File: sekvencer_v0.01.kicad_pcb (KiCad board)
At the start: 2 copper layers, 79.2 x 91.4 mm, 98 parts, among them J1 AVR_ISP_01X06, J10 50V_OUT, J11 BIAS, J12 50V_GND, J13 TERMISTOR, J14 50V_GND, J15 50V_GND, J16 50V_GND, J2 PTT, J3 SWR, J4 POWER, J5 LCD, J6 RX_REL, J7 TX_REL, J8 FAN, J9 50V_IN, Q1 BC857, Q2 Q_NMOS_DGS, Q3 BSS138, Q4 IRLML0030TRPBF, Q5 BBS3002-TL-1E, Q6 BSS138, U1 ATmega328P-AU, U2 LP2950-5.0_TO252, U3 LM2576HVS-12, U4 LTC6101AHS5, Y1 16MHz

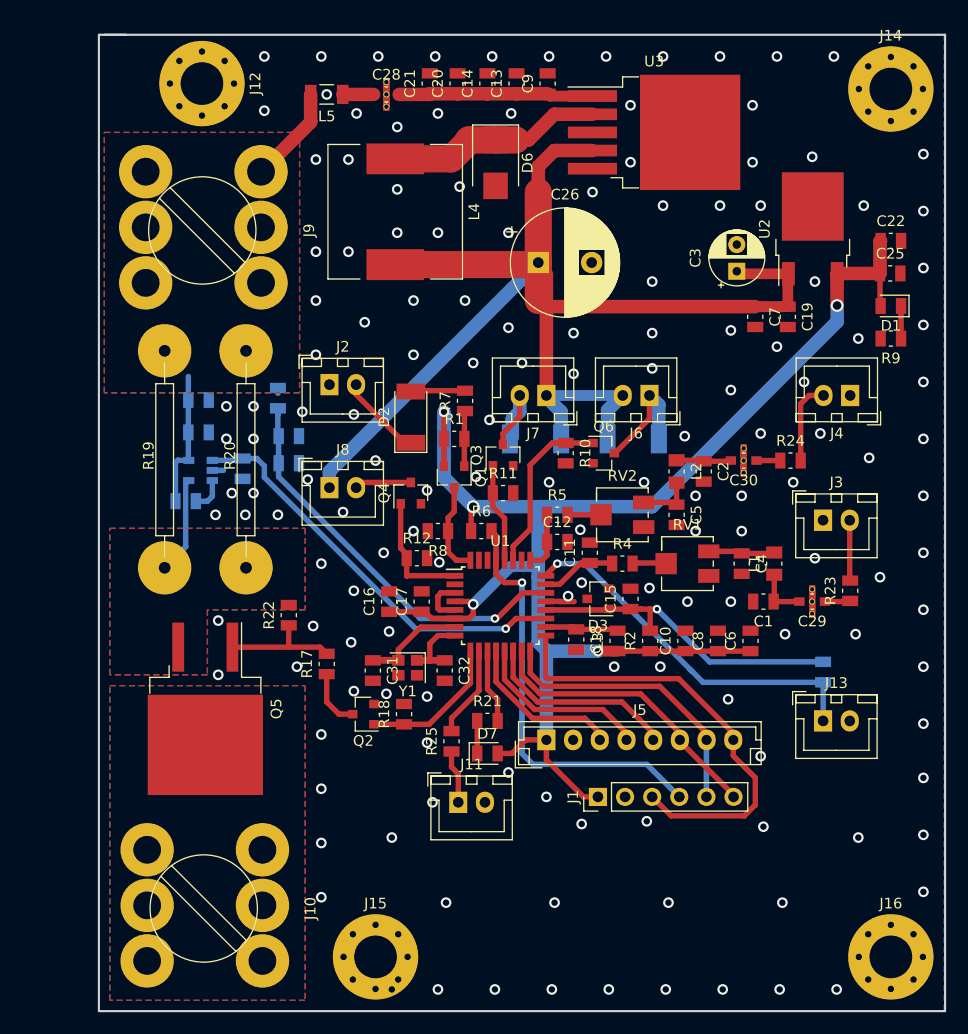
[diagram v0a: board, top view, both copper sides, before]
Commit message: refactored second version, added bias circuit, fixed layout
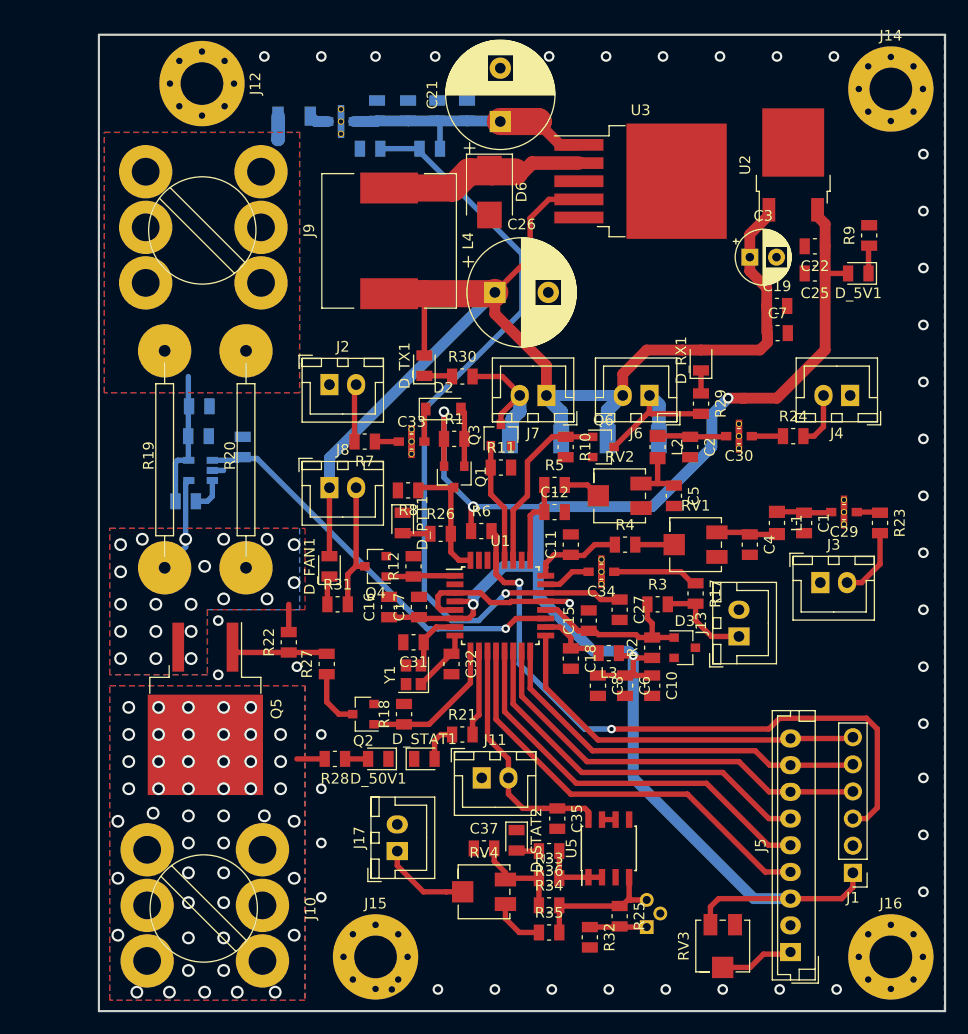
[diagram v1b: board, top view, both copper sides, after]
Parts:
- removed D1: 5V_LED, LED_SMD:LED_0805_2012Metric
- removed D7: STAT_LED, LED_SMD:LED_0805_2012Metric
- added C33: NFM21CC223R1H3D, EMI_Suppression_Filters_Cap_Type:NFM21C_Series, F.Cu at (183.7, 86.4)
- added C34: NFM21CC223R1H3D, EMI_Suppression_Filters_Cap_Type:NFM21C_Series, F.Cu at (201.5, 98.6)
- added C35: 2u2, Capacitor_SMD:C_0805_2012Metric, F.Cu at (197.4, 121.7)
- added C37: 1u, Capacitor_SMD:C_0805_2012Metric, F.Cu at (190.5, 124.5)
- added D_50V1: LH R974-LP-1, LED_SMD:LED_0805_2012Metric, F.Cu at (180.6, 116.1)
- added D_5V1: LH R974-LP-1, LED_SMD:LED_0805_2012Metric, F.Cu at (225.6, 70.6)
- added D_FAN1: LH R974-LP-1, LED_SMD:LED_0805_2012Metric, F.Cu at (176.0, 98.0)
- added D_PTT1: LH R974-LP-1, LED_SMD:LED_0805_2012Metric, F.Cu at (182.9, 94.0)
- added D_RX1: LH R974-LP-1, LED_SMD:LED_0805_2012Metric, F.Cu at (210.8, 78.7)
- added D_STAT1: LH R974-LP-1, LED_SMD:LED_0805_2012Metric, F.Cu at (184.9, 116.1)
- added D_STAT2: LH R974-LP-1, LED_SMD:LED_0805_2012Metric, F.Cu at (193.5, 123.7)
- added D_TX1: LH R974-LP-1, LED_SMD:LED_0805_2012Metric, F.Cu at (184.9, 79.2)
- added J17: BIAS, Connector_JST:JST_XH_B02B-XH-A_1x02_P2.50mm_Vertical, F.Cu at (182.4, 124.7)
- added Q7: BC847, Package_TO_SOT_THT:TO-92, B.Cu at (205.7, 131.8)
- added R26: 1k, Resistor_SMD:R_0805_2012Metric, F.Cu at (186.4, 95.0)
- added R27: 12k, Resistor_SMD:R_0805_2012Metric, F.Cu at (175.8, 107.2)
- added R28: 18k, Resistor_SMD:R_0805_2012Metric, F.Cu at (176.5, 116.1)
- added R29: 3k9, Resistor_SMD:R_0805_2012Metric, F.Cu at (210.8, 82.8)
- added R30: 3k9, Resistor_SMD:R_0805_2012Metric, F.Cu at (188.5, 80.3)
- added R31: 3k9, Resistor_SMD:R_0805_2012Metric, F.Cu at (176.8, 101.6)
- added R32: 2k2, Resistor_SMD:R_0805_2012Metric, F.Cu at (200.4, 132.8)
- added R33: 10R, Resistor_SMD:R_0805_2012Metric, F.Cu at (196.6, 127.3)
- added R34: 1k, Resistor_SMD:R_0805_2012Metric, F.Cu at (196.6, 129.8)
- added R35: 220R, Resistor_SMD:R_0805_2012Metric, F.Cu at (196.6, 132.3)
- added R36: R, Resistor_SMD:R_0805_2012Metric, F.Cu at (196.6, 124.7)
- added RV3: 10k, Potentiometer_SMD:Potentiometer_Bourns_3214J_Horizontal, F.Cu at (212.9, 133.6)
- added RV4: 10k, Potentiometer_SMD:Potentiometer_Bourns_3214J_Horizontal, F.Cu at (190.5, 128.5)
- added U5: LP2951ACD-3.3R2G, Package_SO:SOIC-8_3.9x4.9mm_P1.27mm, F.Cu at (202.2, 124.5)
- C13, C14, C20, C28, C9, L5: moved to B.Cu
- C21: footprint Capacitor_SMD:C_0805_2012Metric -> Capacitor_THT:CP_Radial_D10.0mm_P5.00mm
- C27, R3: moved to F.Cu
- D2: footprint Diode_SMD:D_MELF -> Diode_SMD:D_SOD-123
- J11: value BIAS -> BIAS_DIRECT
- J5: footprint Connector_JST:JST_EH_B08B-EH-A_1x08_P2.50mm_Vertical -> Connector_JST:JST_EH_B09B-EH-A_1x09_P2.50mm_Vertical
- R13: value 330R -> 499R
- R14: value 2k -> 10k
- R17: value 12k -> 22k
- R19, R20: value 0R01 -> 0R005
- R2: value 180R -> 1k
- R25: value 1k -> 1k2
- moved R17 35.2 mm to (210.3, 100.6), turned to 270 degrees
- moved C27 33.9 mm to (203.2, 102.1), turned to 270 degrees
- moved J5 30.3 mm to (219.2, 134.2), turned to 90 degrees
- moved R16 28.0 mm to (179.8, 58.9), turned to 180 degrees
- moved R15 27.4 mm to (185.4, 58.9), turned to 180 degrees
- moved J1 24.9 mm to (225.0, 126.7), turned to 180 degrees
- moved R25 22.7 mm to (203.2, 130.8), turned to 270 degrees
- moved R3 16.7 mm to (206.8, 101.6), turned to 0 degrees
- moved C9 16.2 mm to (180.5, 55.4)
- moved C6 12.5 mm to (203.7, 109.2), turned to 270 degrees
- moved C8 12.0 mm to (201.2, 109.2), turned to 270 degrees
- moved J13 11.2 mm to (214.4, 104.6), turned to 90 degrees
- moved C13 10.5 mm to (183.4, 55.4)
- moved R7 10.1 mm to (179.3, 86.4), turned to 180 degrees
- moved R9 9.86 mm to (226.6, 67.1), turned to 90 degrees
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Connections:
- D2 pad 1: Net-(D2-Pad1) -> Net-(C33-Pad3)
- J1 pad 3: /DB7 -> /RESET
- J1 pad 4: /RESET -> /DB5
- J1 pad 6: /DB5 -> /DB7
- J11 pad 1: Net-(J11-Pad1) -> GND
- J11 pad 2: GND -> /MCU_BIAS
- J13 pad 1: /ADC_TEMP -> Net-(J13-Pad1)
- J2 pad 2: Net-(D2-Pad1) -> Net-(J2-Pad2)
- J5 pad 1: +5V -> Net-(J5-Pad1)
- J5 pad 3: /RS -> +5V
- J5 pad 4: /E -> /RS
- J5 pad 5: /DB4 -> /E
- J5 pad 6: /DB5 -> /DB4
- J5 pad 7: /DB6 -> /DB5
- J5 pad 8: /DB7 -> /DB6
- Q1 pad 1: Net-(Q1-Pad1) -> Net-(D2-Pad2)
- R1 pad 2: Net-(Q1-Pad1) -> Net-(D2-Pad2)
- R15 pad 1: +50V -> Net-(C13-Pad1)
- R17 pad 1: Net-(Q2-Pad3) -> Net-(C34-Pad1)
- R17 pad 2: Net-(Q5-Pad1) -> Net-(J13-Pad1)
- R21 pad 2: /STATUS_LED -> /STATUS_LED1
- R25 pad 1: Net-(J11-Pad1) -> Net-(Q7-Pad3)
- R25 pad 2: /MCU_BIAS -> Net-(Q7-Pad1)
- R3 pad 2: /ADC_TEMP -> Net-(J13-Pad1)
- R7 pad 1: Net-(Q1-Pad1) -> Net-(C33-Pad1)
- R7 pad 2: Net-(D2-Pad2) -> Net-(J2-Pad2)
- U1 pad 10: /MCU_BIAS -> /STATUS_LED1
- U1 pad 11: /STATUS_LED -> /MCU_BIAS
- U1 pad 2: (no net) -> Net-(U1-Pad2)
- U1 pad 23: /ADC_SWR -> /ADC_TEMP
- U1 pad 24: /ADC_TEMP -> /ADC_SWR
- U1 pad 26: (no net) -> Net-(U1-Pad26)
- U1 pad 30: (no net) -> Net-(U1-Pad30)
- U1 pad 31: (no net) -> Net-(U1-Pad31)
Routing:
- net /ADC_UCC: track 37.9 -> 74.0 mm
- net /ADC_TEMP: track 34.9 -> 4.50 mm, vias 1 -> 0
- net /RS: track 15.2 -> 39.9 mm
- net +5V: track 146.6 -> 170.7 mm
- net /RESET: track 39.4 -> 61.3 mm, vias 1 -> 2
- net /E: track 16.8 -> 37.6 mm
- net /DB4: track 18.4 -> 35.4 mm
- net /MCU_BIAS: track 8.56 -> 23.6 mm
- net +2V5: track 30.6 -> 16.8 mm, vias 1 -> 0
- net Net-(Q7-Pad3): track 0.00 -> 12.8 mm
- net /DB5: track 27.4 -> 39.0 mm
- net /DB6: track 26.9 -> 36.7 mm
- net Net-(C37-Pad2): track 0.00 -> 9.08 mm
- net Net-(J13-Pad1): track 0.00 -> 8.89 mm
- net Net-(J17-Pad1): track 0.00 -> 8.50 mm
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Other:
- outline, holes or cut-outs redrawn

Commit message: oficial second version, fixed previous commit
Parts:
- added J18: 50V_GND, MountingHole:MountingHole_3.2mm_M3_Pad_Via, F.Cu at (151.4, 115.3)
- D4, D5: moved to F.Cu
- J12, J14, J16: footprint MountingHole:MountingHole_4mm_Pad_Via -> MountingHole:MountingHole_4.3mm_M4_Pad_Via
- J15: footprint MountingHole:MountingHole_4mm_Pad_Via -> MountingHole:MountingHole_3.2mm_M3_Pad_Via
- moved J15 19.0 mm to (177.8, 115.8)
- moved D_50V1 18.1 mm to (181.6, 134.1)
- moved R28 18.1 mm to (177.3, 134.1)
- moved D5 11.5 mm to (186.9, 78.2), turned to 270 degrees
- moved R29 11.1 mm to (207.0, 72.4), turned to 0 degrees
- moved D4 10.2 mm to (205.0, 75.9)
- moved D_RX1 10.1 mm to (202.9, 72.4), turned to 180 degrees
- moved C32 5.40 mm to (183.9, 111.3), turned to 180 degrees
- moved R30 5.09 mm to (183.4, 80.5)
- moved C34 4.92 mm to (206.2, 99.8)
- moved J17 3.84 mm to (182.9, 128.5), turned to 180 degrees
- moved D_TX1 3.42 mm to (182.6, 76.7)
- moved C27 3.06 mm to (200.9, 100.1), turned to 0 degrees
- moved R18 2.95 mm to (183.4, 114.8), turned to 270 degrees
- moved J1 2.29 mm to (225.0, 124.5)
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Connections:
- J1 pad 3: /RESET -> /DB5
- J1 pad 4: /DB5 -> /DB6
- J1 pad 5: /DB6 -> /DB7
- J1 pad 6: /DB7 -> /RESET
- J13 pad 1: Net-(J13-Pad1) -> GND
- J13 pad 2: GND -> Net-(J13-Pad2)
- R17 pad 2: Net-(J13-Pad1) -> Net-(J13-Pad2)
- R3 pad 2: Net-(J13-Pad1) -> Net-(J13-Pad2)
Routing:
- net /RESET: track 61.3 -> 48.7 mm
- net Net-(J13-Pad1): track 8.89 -> 0.00 mm
- net Net-(J13-Pad2): track 0.00 -> 7.24 mm
- net +12V: track 119.2 -> 125.2 mm
- net Net-(C34-Pad1): track 8.07 -> 2.70 mm
- net /ADC_TEMP: track 4.50 -> 9.79 mm
- net Net-(C32-Pad1): track 5.87 -> 9.41 mm
- net Net-(J17-Pad1): track 8.50 -> 5.62 mm
- net +2V5: track 16.8 -> 14.4 mm
- net Net-(D_STAT1-Pad2): track 3.60 -> 5.66 mm
- net /STATUS_LED1: track 8.09 -> 6.05 mm
- net Net-(D5-Pad2): track 13.1 -> 15.0 mm
- net /MCU_SUPPLY: track 13.6 -> 15.4 mm
- net Net-(Q2-Pad3): track 5.50 -> 3.93 mm
- net /ADC_UCC: track 74.0 -> 72.6 mm
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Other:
- board size 79.2 x 91.4 mm -> 86.4 x 91.4 mm

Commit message: third version, sent to fabrication in allpcb
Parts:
- removed D_STAT2: LH R974-LP-1, LED_SMD:LED_0805_2012Metric
- added C36: NFM21CC223R1H3D, EMI_Suppression_Filters_Cap_Type:NFM21C_Series, F.Cu at (187.3, 133.0)
- added C38: NFM21CC223R1H3D, EMI_Suppression_Filters_Cap_Type:NFM21C_Series, B.Cu at (159.3, 88.5)
- added C39: NFM21CC223R1H3D, EMI_Suppression_Filters_Cap_Type:NFM21C_Series, B.Cu at (156.5, 85.7)
- added D_3V3: LH R974-LP-1, LED_SMD:LED_0805_2012Metric, F.Cu at (193.5, 123.6)
- added J19: 50V_GND, MountingHole:MountingHole_3.2mm_M3_Pad_Via, F.Cu at (151.4, 134.6)
- added L6: BLM31PG500SN1L, Capacitor_SMD:C_1206_3216Metric, F.Cu at (182.4, 133.1)
- added L7: BLM31PG500SN1L, Capacitor_SMD:C_1206_3216Metric, B.Cu at (156.5, 91.4)
- added L8: BLM31PG500SN1L, Capacitor_SMD:C_1206_3216Metric, B.Cu at (159.3, 84.3)
- added TP1: ADC_UCC, TestPoint:TestPoint_Pad_D2.0mm, F.Cu at (199.9, 99.9)
- added TP2: +5V, TestPoint:TestPoint_Pad_D2.0mm, F.Cu at (222.5, 75.0)
- added TP3: +12V, TestPoint:TestPoint_Pad_D2.0mm, F.Cu at (211.2, 69.8)
- added TP4: ADC ICC, TestPoint:TestPoint_Pad_D2.0mm, B.Cu at (170.6, 90.0)
- added TP5: GND, TestPoint:TestPoint_Pad_D2.0mm, F.Cu at (199.7, 76.5)
- C31, C32: value 22p -> 15p
- J12, J14, J16: footprint MountingHole:MountingHole_4.3mm_M4_Pad_Via -> MountingHole:MountingHole_3.2mm_M3_Pad_Via
- R36: value R -> 470R
- Y1: footprint Crystal:Crystal_SMD_2520-4Pin_2.5x2.0mm -> KLALIB_Crystal:Crystal_SMD_2520-4Pin_2.5x2.0mm
- moved J12 11.7 mm to (152.4, 53.3)
- moved C23 6.20 mm to (168.9, 86.6), turned to 270 degrees
- moved R14 5.36 mm to (164.4, 90.9), turned to 90 degrees
- moved R31 3.81 mm to (176.8, 97.8)
- moved R7 3.78 mm to (181.9, 83.6), turned to 90 degrees
- moved D_50V1 3.69 mm to (181.4, 137.8)
- moved R28 3.69 mm to (177.0, 137.8)
- moved D_FAN1 3.31 mm to (175.8, 94.7)
- moved J2 3.14 mm to (178.3, 78.9), turned to 180 degrees
- moved C32 3.07 mm to (186.2, 109.3), turned to 270 degrees
- moved J3 2.90 mm to (224.8, 100.3), turned to 180 degrees
- moved J8 2.62 mm to (178.3, 89.4), turned to 180 degrees
- moved J11 2.61 mm to (192.8, 118.6), turned to 180 degrees
- moved U4 2.55 mm to (162.9, 86.7), turned to 90 degrees
- moved C24 2.46 mm to (166.1, 86.5), turned to 270 degrees
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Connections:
- C35 pad 1: /MCU_BIAS -> +5V
- J11 pad 1: GND -> /MCU_BIAS
- J11 pad 2: /MCU_BIAS -> GND
- J2 pad 1: GND -> Net-(J2-Pad1)
- J2 pad 2: Net-(J2-Pad2) -> GND
- J3 pad 1: GND -> Net-(J3-Pad1)
- J3 pad 2: Net-(J3-Pad2) -> GND
- J8 pad 1: +12V -> Net-(J8-Pad1)
- J8 pad 2: Net-(J8-Pad2) -> +12V
- Q4 pad 3: Net-(J8-Pad2) -> Net-(J8-Pad1)
- Q5 pad 3: Net-(Q5-Pad3) -> Net-(L7-Pad1)
- R13 pad 1: Net-(R13-Pad1) -> Net-(C38-Pad1)
- R13 pad 2: +50V -> Net-(R13-Pad2)
- R19 pad 1: Net-(Q5-Pad3) -> Net-(L7-Pad1)
- R20 pad 1: Net-(Q5-Pad3) -> Net-(L7-Pad1)
- R22 pad 2: Net-(Q5-Pad3) -> Net-(L7-Pad1)
- R23 pad 2: Net-(J3-Pad2) -> Net-(J3-Pad1)
- R31 pad 2: Net-(J8-Pad2) -> Net-(J8-Pad1)
- R7 pad 2: Net-(J2-Pad2) -> Net-(J2-Pad1)
- RV4 pad 2: Net-(J17-Pad1) -> Net-(C36-Pad1)
- U4 pad 3: Net-(R13-Pad1) -> Net-(R13-Pad2)
- U4 pad 4: Net-(Q5-Pad3) -> Net-(C39-Pad1)
- U5 pad 3: Net-(U5-Pad3) -> /MCU_BIAS
- U5 pad 8: /MCU_BIAS -> +5V
- Y1 pad 2: Net-(C31-Pad1) -> GND
- Y1 pad 3: (no net) -> Net-(C31-Pad1)
- Y1 pad 4: (no net) -> GND
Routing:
- net GND: track 16.8 -> 35.6 mm, vias 41 -> 225
- net +5V: track 172.1 -> 186.0 mm, vias 5 -> 6
- net Net-(J8-Pad2): track 12.1 -> 0.00 mm
- net Net-(Q5-Pad3): track 11.7 -> 0.00 mm, vias 21 -> 0
- net /MCU_BIAS: track 23.6 -> 34.4 mm
- net Net-(J8-Pad1): track 0.00 -> 10.4 mm
- net Net-(J3-Pad1): track 0.00 -> 7.47 mm
- net Net-(J3-Pad2): track 6.71 -> 0.00 mm
- net Net-(C39-Pad1): track 0.00 -> 6.60 mm
- net Net-(J2-Pad1): track 0.00 -> 5.83 mm
- net Net-(J2-Pad2): track 5.40 -> 0.00 mm
- net Net-(L7-Pad1): track 0.00 -> 4.91 mm, vias 0 -> 21
- net Net-(C36-Pad1): track 0.00 -> 4.46 mm
- net /ADC_ICC: track 38.0 -> 42.1 mm
- net Net-(R13-Pad2): track 0.00 -> 3.82 mm
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- added copper zone on B.Cu, net Net-(L7-Pad1)
- added copper zone on F.Cu, net Net-(L7-Pad1)
- removed copper zone on B.Cu, net Net-(Q5-Pad3)
- removed copper zone on F.Cu, net Net-(Q5-Pad3)
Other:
- board text added: "+12V"
- board text added: "+50 V OUT"
- board text added: "+50V IN"
- board text added: "+5V"
- board text added: "ADC"
- board text added: "ADC ICC"
- board text added: "BIAS"
- board text added: "BIAS DIRECT"
- board text added: "FAN"
- board text added: "ISP"
- board text added: "LCD"
- board text added: "POWER"
- board text added: "PTT"
- board text added: "REL1"
- board text added: "REL2"
- board text added: "SWR"
- board text added: "TEMP"
- board text added: "UCC"

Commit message: added some docs and outputs
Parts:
- D2, D4, D5: value D -> 1N4148
- L1, L2: value 560n -> 470n
- Q2: value Q_NMOS_DGS -> BSS138

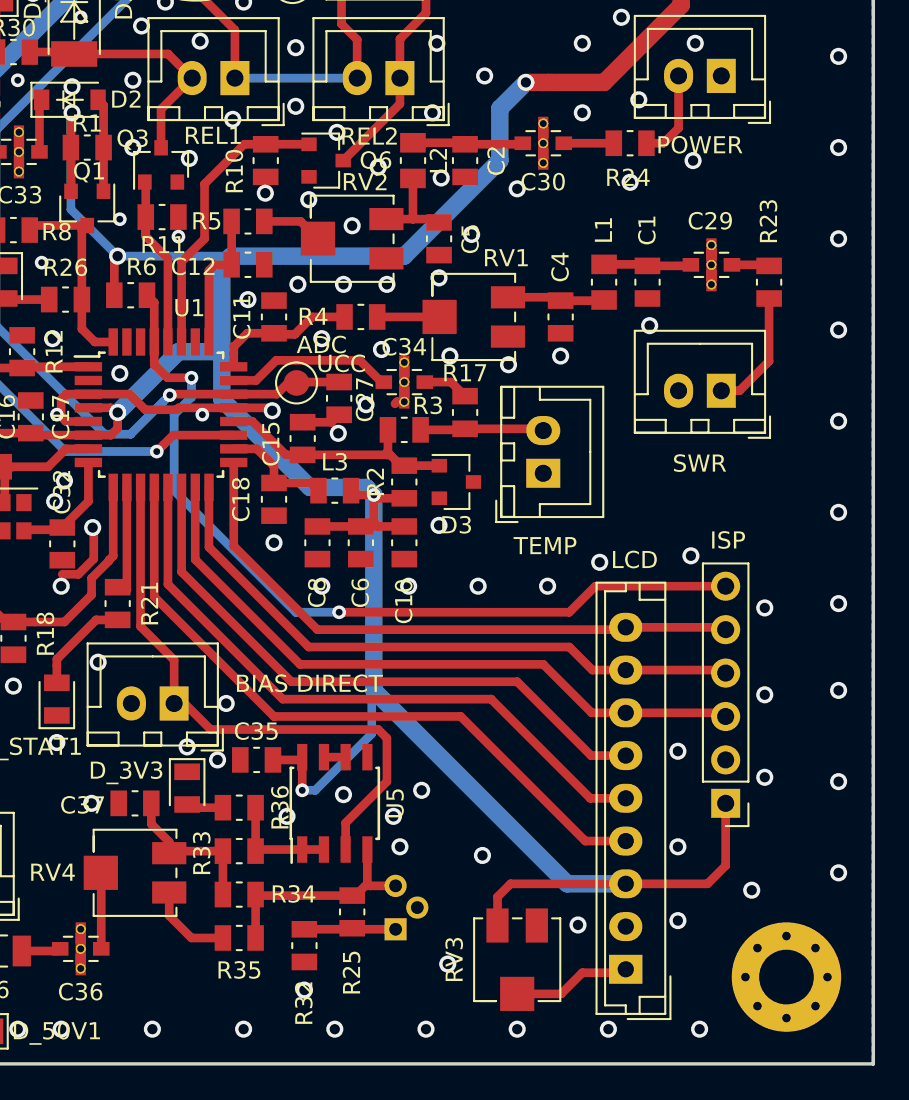
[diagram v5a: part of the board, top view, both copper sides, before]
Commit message: first revision, added resistor and diode in bias circuit
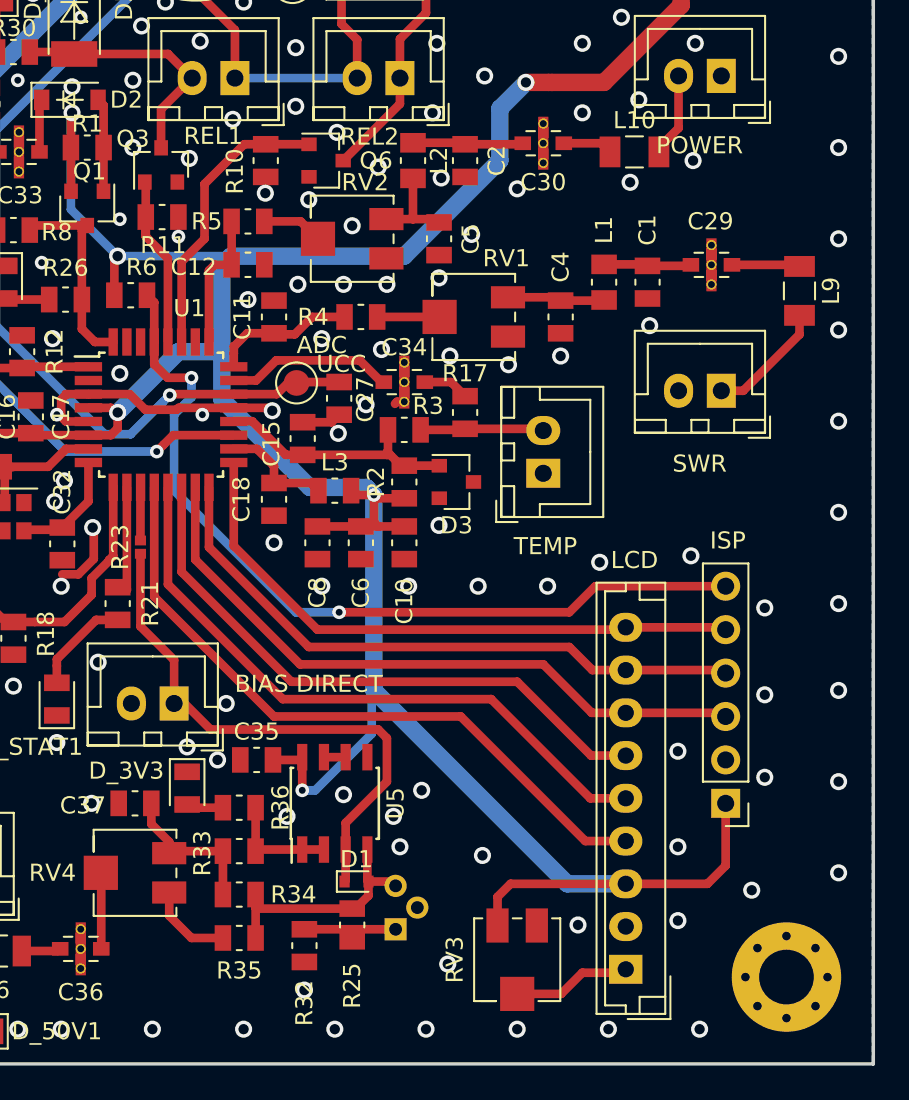
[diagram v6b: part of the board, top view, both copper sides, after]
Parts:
- removed R24: 1k, Resistor_SMD:R_0805_2012Metric
- added D1: BAS7002VH6327XTSA1, Diode_SMD:D_SOD-523, F.Cu at (203.5, 129.0)
- added L10: BLM31PG500SN1L, Capacitor_SMD:C_1206_3216Metric, F.Cu at (219.7, 86.4)
- added L9: BLM31PG500SN1L, Capacitor_SMD:C_1206_3216Metric, F.Cu at (229.4, 94.5)
- R23: value 1k -> 100k; footprint Resistor_SMD:R_0805_2012Metric -> Resistor_SMD:R_0402_1005Metric
- Y1: value 16MHz -> LFXTAL071268CUTT 16MHz
- moved R23 39.9 mm to (190.8, 109.5), turned to 90 degrees
- moved R25 0.76 mm to (203.2, 131.6)
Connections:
- J11 pad 1: /MCU_BIAS -> Net-(D1-Pad1)
- J14 pad 1: GND -> Net-(J14-Pad1)
- J15 pad 1: GND -> Net-(J15-Pad1)
- J16 pad 1: GND -> Net-(J16-Pad1)
- J19 pad 1: GND -> Net-(J19-Pad1)
- R23 pad 1: Net-(C29-Pad1) -> Net-(D1-Pad1)
- R23 pad 2: Net-(J3-Pad1) -> /MCU_BIAS
- U5 pad 3: /MCU_BIAS -> Net-(D1-Pad1)
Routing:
- net Net-(D1-Pad1): track 0.00 -> 32.4 mm
- net /MCU_BIAS: track 34.4 -> 3.11 mm
- net Net-(C29-Pad1): track 2.20 -> 3.99 mm
- net Net-(D1-Pad2): track 12.8 -> 14.0 mm
- net Net-(J4-Pad2): track 5.17 -> 4.18 mm
- net Net-(Q7-Pad1): track 5.38 -> 6.03 mm
